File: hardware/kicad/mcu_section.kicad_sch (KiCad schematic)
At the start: 15 parts, among them J3 Conn_01x08_Socket, U6 BME680, U7 ESP32-C6-WROOM-1-N8

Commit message: hardware: MCU components
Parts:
- added C14: 1uF, PCM_JLCPCB:C_0603, symbol Device:C
- added C15, C16: 0.1uF, PCM_JLCPCB:C_0603, symbol Device:C
- added C17: 22uF, PCM_JLCPCB:C_0603, symbol Device:C
- added C18: C, PCM_JLCPCB:C_0603, symbol Device:C
- added IC1: AS312, AS312, symbol AS312:AS312
- added Q1: AO3400A, Package_TO_SOT_SMD:SOT-23, symbol Transistor_FET:AO3400A
- added R15: 1K, PCM_JLCPCB:R_0603, symbol Device:R
- added R18: 220, PCM_JLCPCB:R_0603, symbol Device:R
- added R19: 10K, PCM_JLCPCB:R_0603, symbol Device:R
- added SW1, SW2: SW_Push, Button_Switch_SMD:SW_Push_SPST_NO_Alps_SKRK, symbol Switch:SW_Push
- added Y1: 32.768 kHz, Crystal:Crystal_SMD_3225-4Pin_3.2x2.5mm, symbol Device:Crystal
- R13: value R -> 1K
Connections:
- net +3.3V: now also R13.1, U7.2 (3V3), C16.2, C17.1, IC1.1 (VDD), R15.1
- net BL: now also Q1.3 (D)
- net CLK: now also J3.5 (Pin_5)
- net CS: now also J3.2 (Pin_2)
- net DIN: now also J3.4 (Pin_4)
- net D/C: now also J3.3 (Pin_3)
- net GND: now also C14.2, C15.2, C16.1, C17.2, IC1.3 (VSS), Q1.2 (S), R19.1, SW1.1, SW2.2
- net at R13.2: now also U7.3 (EN), C14.1, C15.1, SW1.2
- net IO8: now reaches U7.10 (IO8)
- net IO8: now also R15.2
- net D-: now reaches U7.13 (IO12)
- net D+: now reaches U7.14 (IO13)
- net IO9: now reaches U7.15 (IO9)
- net IO9: now also SW2.1
- new net: Q1.1 (G), R18.2, R19.2
- new net REL: IC1.2 (REL)
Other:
- note added: "Change so it opens for pwm only when human detect"
- note removed: "Bootloader buttons"
- note removed: "PIR sensor"
- moved on the sheet: D14, R13

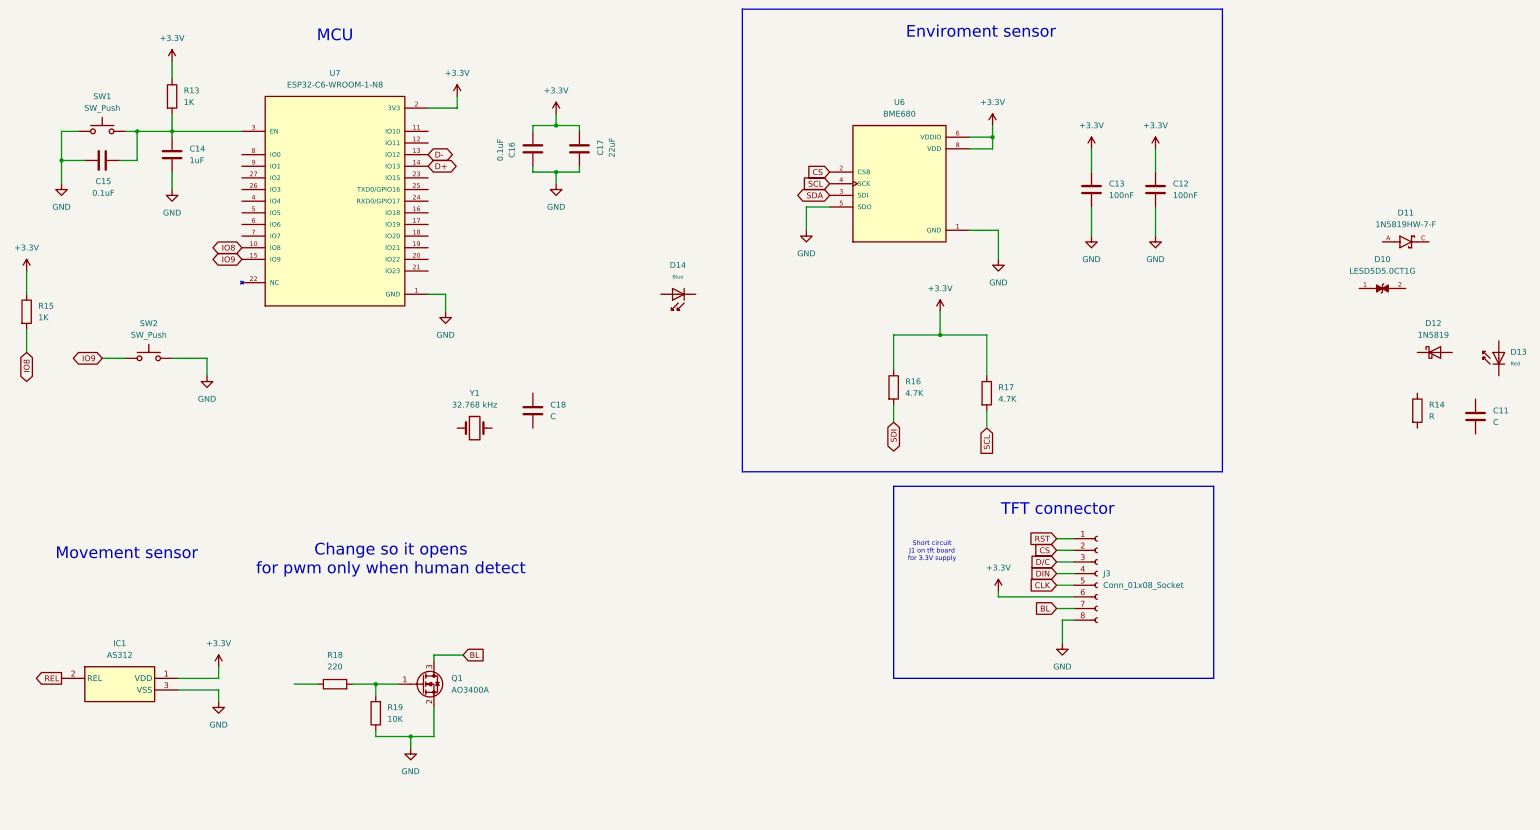
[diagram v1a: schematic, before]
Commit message: hardware: movement sensor
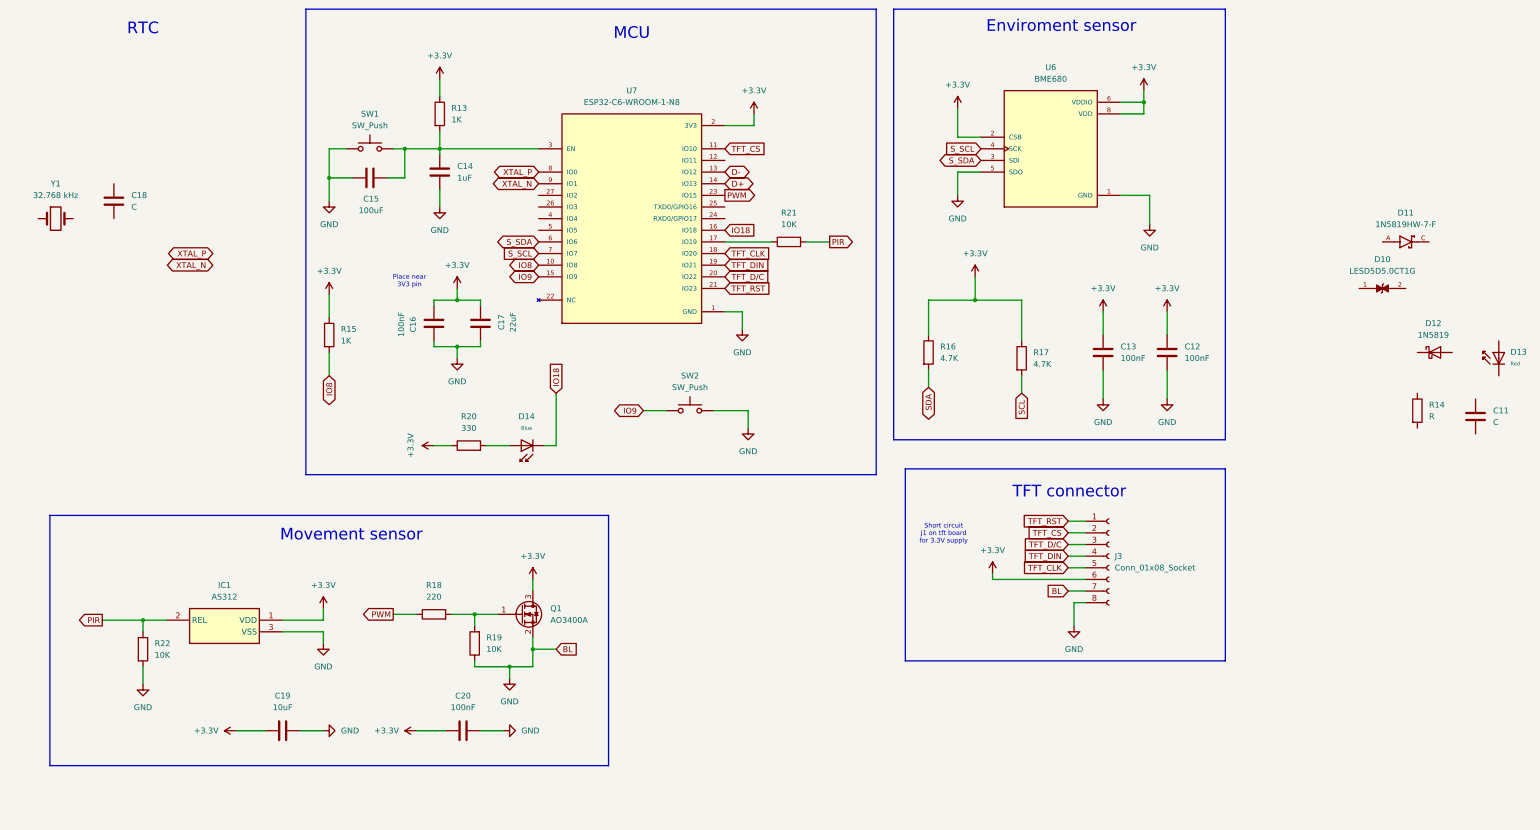
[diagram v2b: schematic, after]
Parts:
- added C19: 10uF, PCM_JLCPCB:C_0603, symbol Device:C
- added C20: 100nF, PCM_JLCPCB:C_0603, symbol Device:C
- added R20: 330, PCM_JLCPCB:R_0603, symbol Device:R
- added R21, R22: 10K, PCM_JLCPCB:R_0603, symbol Device:R
- C15: value 0.1uF -> 100uF
- C16: value 0.1uF -> 100nF
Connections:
- net CLK is gone; now on net TFT_CLK: J3.5 (Pin_5)
- net DIN is gone; now on net TFT_DIN: J3.4 (Pin_4)
- net D/C is gone; now on net TFT_D/C: J3.3 (Pin_3)
- net RST is gone; now on net TFT_RST: J3.1 (Pin_1)
- net SDI is gone; now on net SDA: R16.2
- net +3.3V: now also Q1.3 (D), U6.2 (CSB), C19.1, C20.1, R20.1
- net GND: now also J3.7 (Pin_7), C19.2, C20.2, R22.2
- net SCL: no longer U6.4 (SCK)
- net SDA: no longer U6.3 (SDI)
- net PWM: now reaches R18.1
- net PWM: now also U7.23 (IO15)
- net IO18: now reaches D14.1
- net IO18: now also U7.16 (IO18)
- net at D14.2: now also R20.2
- net TFT_CS: now reaches U7.11 (IO10)
- net TFT_CS: now also J3.2 (Pin_2)
- net at U7.17 (IO19): now also R21.1
- net TFT_CLK: now reaches U7.18 (IO20)
- net TFT_DIN: now reaches U7.19 (IO21)
- net TFT_D/C: now reaches U7.20 (IO22)
- net TFT_RST: now reaches U7.21 (IO23)
- net S_SDA: now reaches U7.6 (IO6)
- net S_SDA: now also U6.3 (SDI)
- net S_SCL: now reaches U7.7 (IO7)
- net S_SCL: now also U6.4 (SCK)
- net XTAL_P: now reaches U7.8 (IO0)
- net XTAL_N: now reaches U7.9 (IO1)
- removed net BL: J3.7 (Pin_7), Q1.3 (D)
- removed net CS: J3.2 (Pin_2), U6.2 (CSB)
- net REL renamed PIR
- net PIR: now also R21.2, R22.1
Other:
- note added: "Place near 3V3 pin"
- note added: "RTC"
- note removed: "Change so it opens for pwm only when human detect"
- moved on the sheet: C12, C13, C14, C15, C16, C17, C18, D14, IC1, J3, Q1, R13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

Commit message: hardware: battery voltage reading and caps
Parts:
- removed C11, C18: C, PCM_JLCPCB:C_0603, symbol Device:C
- removed D11: 1N5819HW-7-F, 1N5819HW-7-F:SOD3715X145N, symbol 1N5819HW-7-F:1N5819HW-7-F
- removed D12: 1N5819, Diode_THT:D_DO-41_SOD81_P10.16mm_Horizontal, symbol Diode:1N5819
- removed D13: Red, PCM_JLCPCB:D_0603, symbol PCM_JLCPCB-Diodes:LED,0603,Red
- removed R14: R, PCM_JLCPCB:R_0603, symbol Device:R
- added C13, C14: 12pF, PCM_JLCPCB:C_0603, symbol Device:C
- added H1, H2, H3, H4: MountingHole, MountingHole:MountingHole_2.2mm_M2, symbol Mechanical:MountingHole
- added R17: 10M, PCM_JLCPCB:R_0603, symbol Device:R
- added R24: 4.7K, PCM_JLCPCB:R_0603, symbol Device:R
- C19: renamed from C17; value 22uF -> 1uF
- D8: renamed from D10; footprint LESD5D5.0CT1G:TVS_LESD5D5.0CT1G -> Diode_SMD:TVS_LESD5D5.0CT1G
- IC1: footprint AS312 -> Sensor:AS312
- U3: renamed from U7; footprint ESP32-C6-WROOM-1-N8:XCVR_ESP32-C6-WROOM-1-N8 -> Module:XCVR_ESP32-C6-WROOM-1-N8
- U4: renamed from U6; footprint BME680:PSON80P300X300X100-8N -> Package_LGA:Bosch_LGA-8_3x3mm_P0.8mm_ClockwisePinNumbering
- Y1: ESR (none) -> ≤70k
- renumbered C19 to C15, C15 to C16, C16 to C17, C14 to C18, C13 to C21, C12 to C22, D14 to D7, Q1 to Q3, R22 to R18, R15 to R19, R13 to R20, R20 to R21, R18 to R22, R19 to R23, R21 to R25, R16 to R26, R17 to R27
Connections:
- net SCL is gone; now on net S_SCL: R27.2
- net SDA is gone; now on net S_SDA: R26.2
- net +3.3V: now also D8.2, R24.2; no longer Q3.3 (D)
- net GND: now also D8.1, C13.1, C14.1; no longer J3.7 (Pin_7)
- net XTAL_N: now also Y1.1, C14.2, R17.2
- net XTAL_P: now also Y1.2, C13.2, R17.1
- net BAT_CTRL: now reaches U3.12 (IO11)
- net BAT_ADC: now reaches U3.26 (IO3)
- new net BL: J3.7 (Pin_7), Q3.3 (D), R24.1
- no-connect marks 0 -> 5
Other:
- note added: "Mountings"
- company: (none) -> Glitch
- title: (none) -> Weather station - MCU section
- moved on the sheet: C15, C16, C17, C18, C19, C20, D7, D8, IC1, Q3, R18, R19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

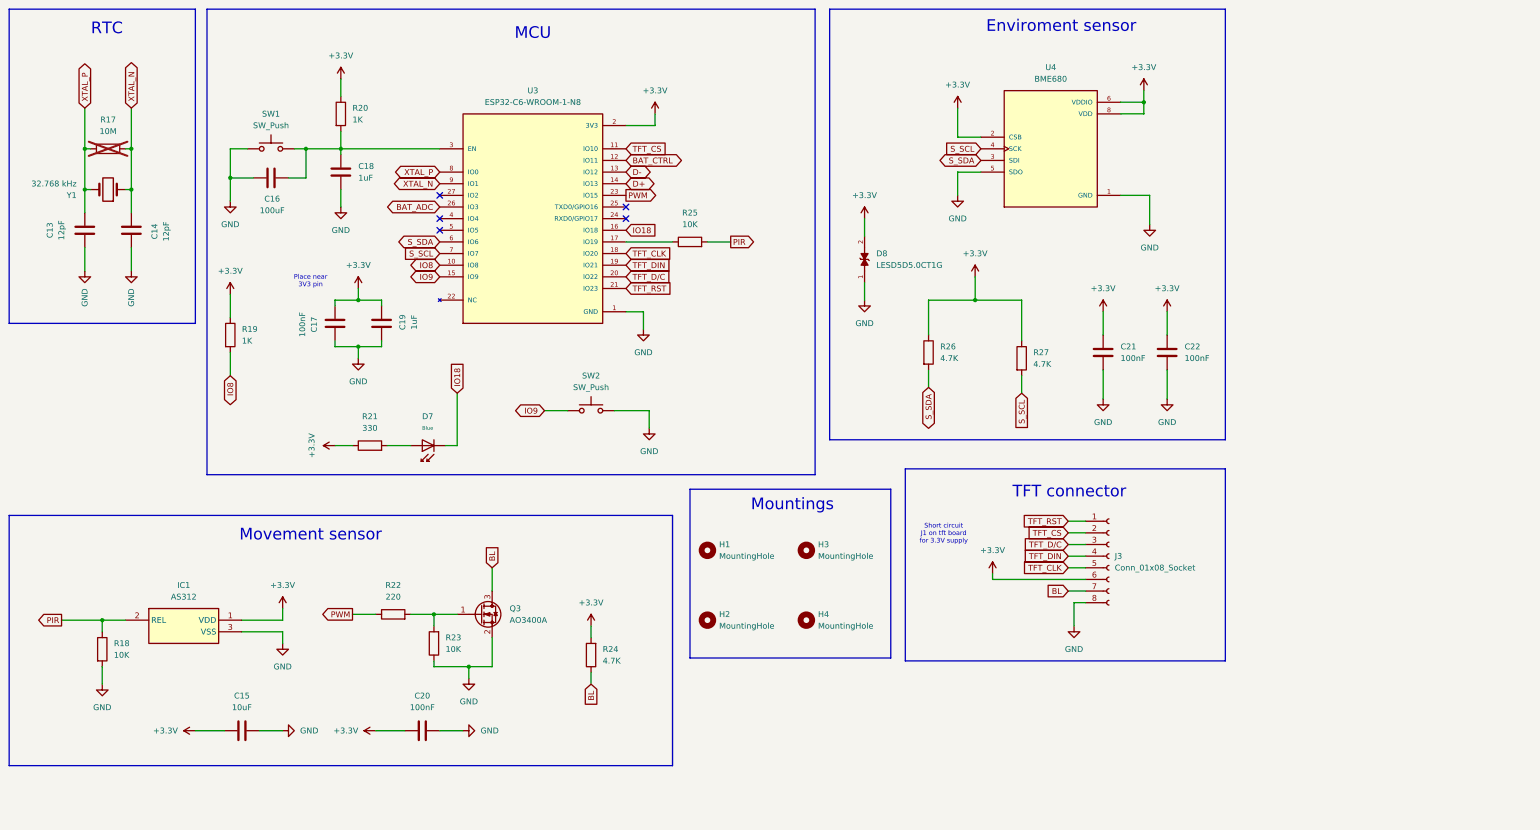
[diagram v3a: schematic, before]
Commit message: hardware: modfied wiring
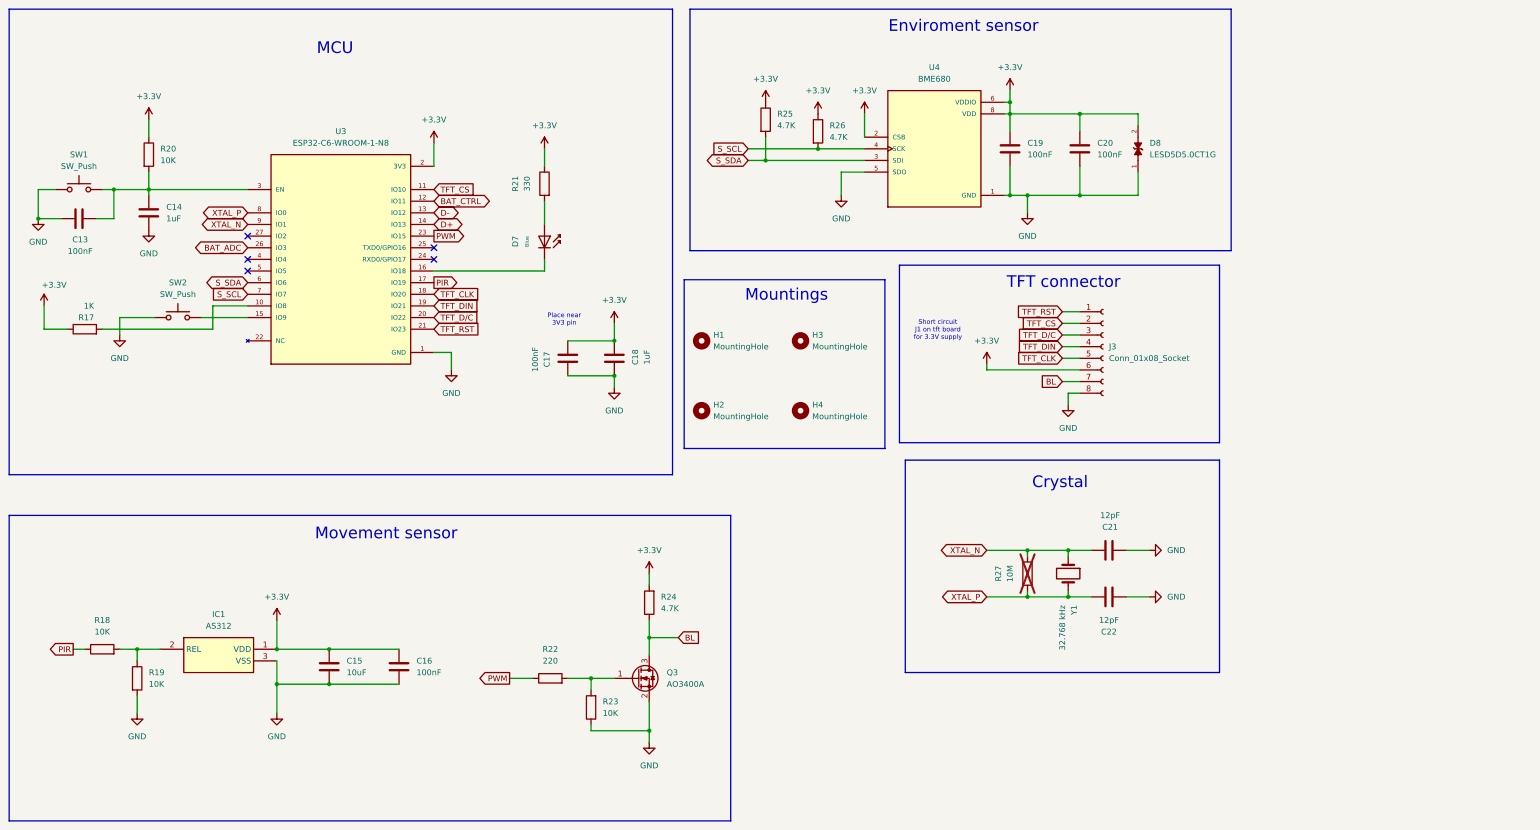
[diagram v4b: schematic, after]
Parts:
- removed R27: 4.7K, PCM_JLCPCB:R_0603, symbol Device:R
- added R25: 4.7K, PCM_JLCPCB:R_0603, symbol Device:R
- C13: renamed from C16; value 100uF -> 100nF
- R20: value 1K -> 10K
- renumbered C18 to C14, C20 to C16, C19 to C18, C21 to C19, C22 to C20, C14 to C21, C13 to C22, R19 to R17, R25 to R18, R18 to R19, R17 to R27
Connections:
- net +3.3V: now also C15.2, C16.2, R25.1; no longer C15.1, C16.1
- net GND: now also C15.1, C16.1; no longer C15.2, C16.2
- net PIR: now also R18.1, U3.17 (IO19); no longer IC1.2 (REL), R18.2, R19.1
- net S_SCL: now also R26.2
- net S_SDA: now also R25.2; no longer R26.2
- net IO18: no longer names the net of D7.1, U3.16 (IO18)
- net IO8: no longer names the net of R17.2, U3.10 (IO8)
- net IO9: no longer names the net of SW2.1, U3.15 (IO9)
- new net: IC1.2 (REL), R18.2, R19.1
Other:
- note added: "Crystal"
- note removed: "RTC"
- moved on the sheet: C13, C14, C15, C16, C17, C18, C19, C20, C21, C22, D7, D8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

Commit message: hardware: ldr voltage divider
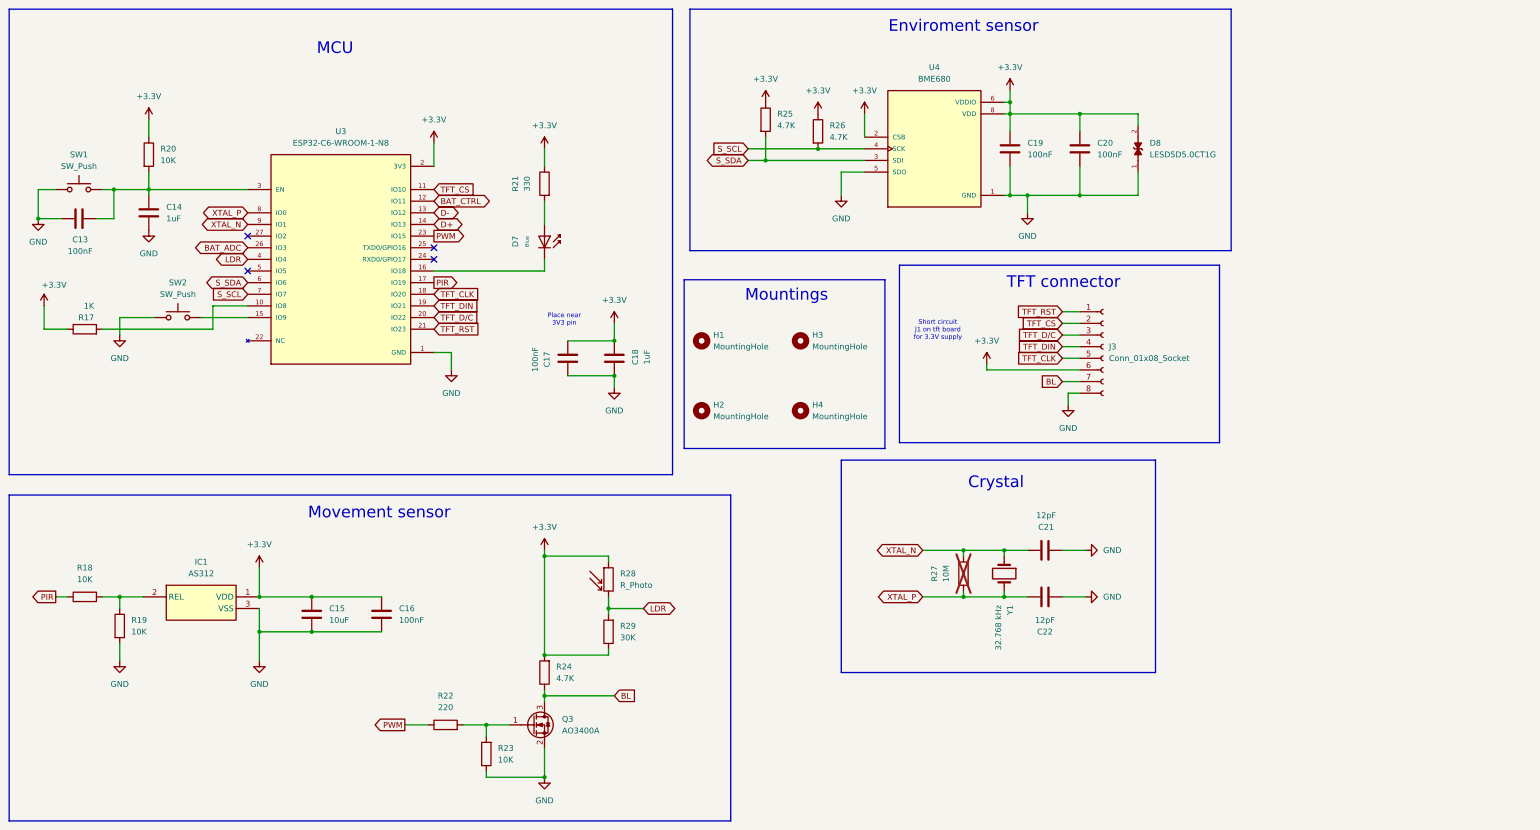
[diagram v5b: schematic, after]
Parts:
- added R28: R_Photo, OptoDevice:R_LDR_5.0x4.1mm_P3mm_Vertical, symbol Device:R_Photo
- added R29: 30K, PCM_JLCPCB:R_0603, symbol Device:R
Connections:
- net +3.3V: now also R28.1, R29.1
- net LDR: now reaches U3.4 (IO4)
- net LDR: now also R28.2, R29.2
- no-connect marks 5 -> 4
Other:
- moved on the sheet: C15, C16, C21, C22, IC1, Q3, R18, R19, R22, R23, R24, R27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

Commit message: fix: incorrect values and missing wirings
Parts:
- added R21, R22, R25, R26: 100K, PCM_JLCPCB:R_0603, symbol Device:R
- added TP4: TP_+3V3, TestPoint:TestPoint_Pad_D1.5mm, symbol Connector:TestPoint
- renumbered C13 to C14, C14 to C15, C15 to C16, C16 to C17, C17 to C18, C18 to C19, C19 to C20, C20 to C23, R22 to R23, R23 to R24, R21 to R27, R24 to R28, R28 to R29, R29 to R30, R25 to R31, R26 to R32, R27 to R33
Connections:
- net +3.3V: no longer R30.1
- net GND: now also R30.1, R21.2, R22.2, R26.2
- net CHG_EN2: now reaches U3.24 (RXD0/GPIO17)
- net CHG_EN2: now also R22.1
- net CHG_EN1: now reaches U3.27 (IO2)
- net CHG_EN1: now also R21.1
- net VBUS_SENSE: now reaches U3.5 (IO5)
- net VBUS_SENSE: now also R25.2, R26.1, TP4.1
- new net +5V: R25.1
- no-connect marks 4 -> 2
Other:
- moved on the sheet: C14, C15, C18, C19, D7, R17, R20, R27, SW1, SW2, U3

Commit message: feat: manufacturer part numbers
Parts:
- C14: LCSC (none) -> C2169129
- C15, C19: LCSC (none) -> C92806
- C16: LCSC (none) -> C49326611
- C17, C18, C20, C23: LCSC (none) -> C1590
- C21, C22: LCSC (none) -> C38523
- D8: LCSC (none) -> C5246195
- IC1: LCSC (none) -> C90465
- J3: LCSC (none) -> C27438
- Q3: LCSC (none) -> C20917
- R17: LCSC (none) -> C25623
- R18, R19, R20, R24: LCSC (none) -> C15401
- R21: LCSC (none) -> C1226
- R22, R25, R30, R31: LCSC (none) -> C15458
- R23: LCSC (none) -> C22104
- R26: LCSC (none) -> C22984
- R27, R28: LCSC (none) -> C25999
- R29: footprint OptoDevice:R_LDR_5.0x4.1mm_P3mm_Vertical -> OptoDevice:R_LDR_5.1x4.3mm_P3.4mm_Vertical; LCSC (none) -> C10081
- R32: LCSC (none) -> C14675
- R33: LCSC (none) -> C26097
- SW1, SW2: LCSC (none) -> C720477
- U3: LCSC (none) -> C5366877
- U4: LCSC (none) -> C125972
- Y1: footprint Crystal:Crystal_SMD_3225-4Pin_3.2x2.5mm -> Crystal:Crystal_SMD_0603-2Pin_6.0x3.5mm; LCSC (none) -> C97606
